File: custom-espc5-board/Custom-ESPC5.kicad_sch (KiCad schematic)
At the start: 43 parts, among them J1 Screw_Terminal_01x02, J10 Barrel_Jack, J12 Conn_01x05, J13 Conn_01x05, J2 Conn_01x03, J3 Conn_01x03, J4 USB_C_Receptacle_USB2.0_14P, J5 Conn_01x03, J6 Screw_Terminal_01x03, SW1 SW_Nidec_CAS-120A1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

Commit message: s3 devboard + imu
austin yun
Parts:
- removed J2, J3: Conn_01x03, Connector_JST:JST_XH_S3B-XH-A-1_1x03_P2.50mm_Horizontal, symbol Connector_Generic:Conn_01x03
- removed U1: ESP32-C5-WROOM-1U, PCM_Espressif:ESP32-C5-WROOM-1U, symbol PCM_Espressif:ESP32-C5-WROOM-1U
- added C8: 10nF, Capacitor_SMD:C_0402_1005Metric, symbol Device:C
- added U1: ICM-42670-P, footprints:LGA14_2.5X3X0.76_IVS, symbol imu:ICM-42670-P
- added U6: ESP32-S3-WROOM-1, RF_Module:ESP32-S3-WROOM-1, symbol RF_Module:ESP32-S3-WROOM-1
- C3: value 0.1µ -> 0.1µF
- C4: value 0.1µ -> 2.2µF
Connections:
- net SIG1 is gone; now on net +3.3V: C3.1
- net SIG2 is gone; now on net +3.3V: C4.1
- net +3.3V: now also C8.1, U1.5 (VDDIO), U1.8 (VDD), U6.2 (3V3)
- net A1: now also U6.20 (IO12)
- net A2: now also U6.19 (IO11)
- net B1: now also U6.8 (IO15)
- net B2: now also U6.7 (IO7)
- net CAN RX: now also U6.39 (IO1)
- net CAN TX: now also U6.38 (IO2)
- net CHIP_PU: now also U6.3 (EN)
- net GND: now also C8.2, U1.6 (GND), U6.1 (GND), U6.40 (GND), U6.41 (GND)
- net IDX1: now also U6.21 (IO13)
- net IDX2: now also U6.9 (IO16)
- net UART RX: now also U6.36 (RXD0)
- net UART TX: now also U6.37 (TXD0)
- net WS2812: now also U6.10 (IO17)
- net GPIO28 renamed GPIO0
- net GPIO0: now also U6.27 (IO0)
- net I2C SCL renamed SCL
- net SCL: now also U1.13 (AP_SCL/AP_SCLK), U6.17 (IO9)
- net I2C SDA renamed SDA
- net SDA: now also U1.14 (AP_SDA/AP_SDIO/AP_SDI), U6.18 (IO10)
- no-connect marks 11 -> 16
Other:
- note added: "IMU"
- note added: "quack"
- note removed: "Analog"
- note removed: "Analog 1"
- note removed: "Analog 2"
- note removed: "Vcc"
- note removed: "wolfwood"
- moved on the sheet: C5, C6, D2, D4, J1, J12, J13, J4, J5, J6, R17, R18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

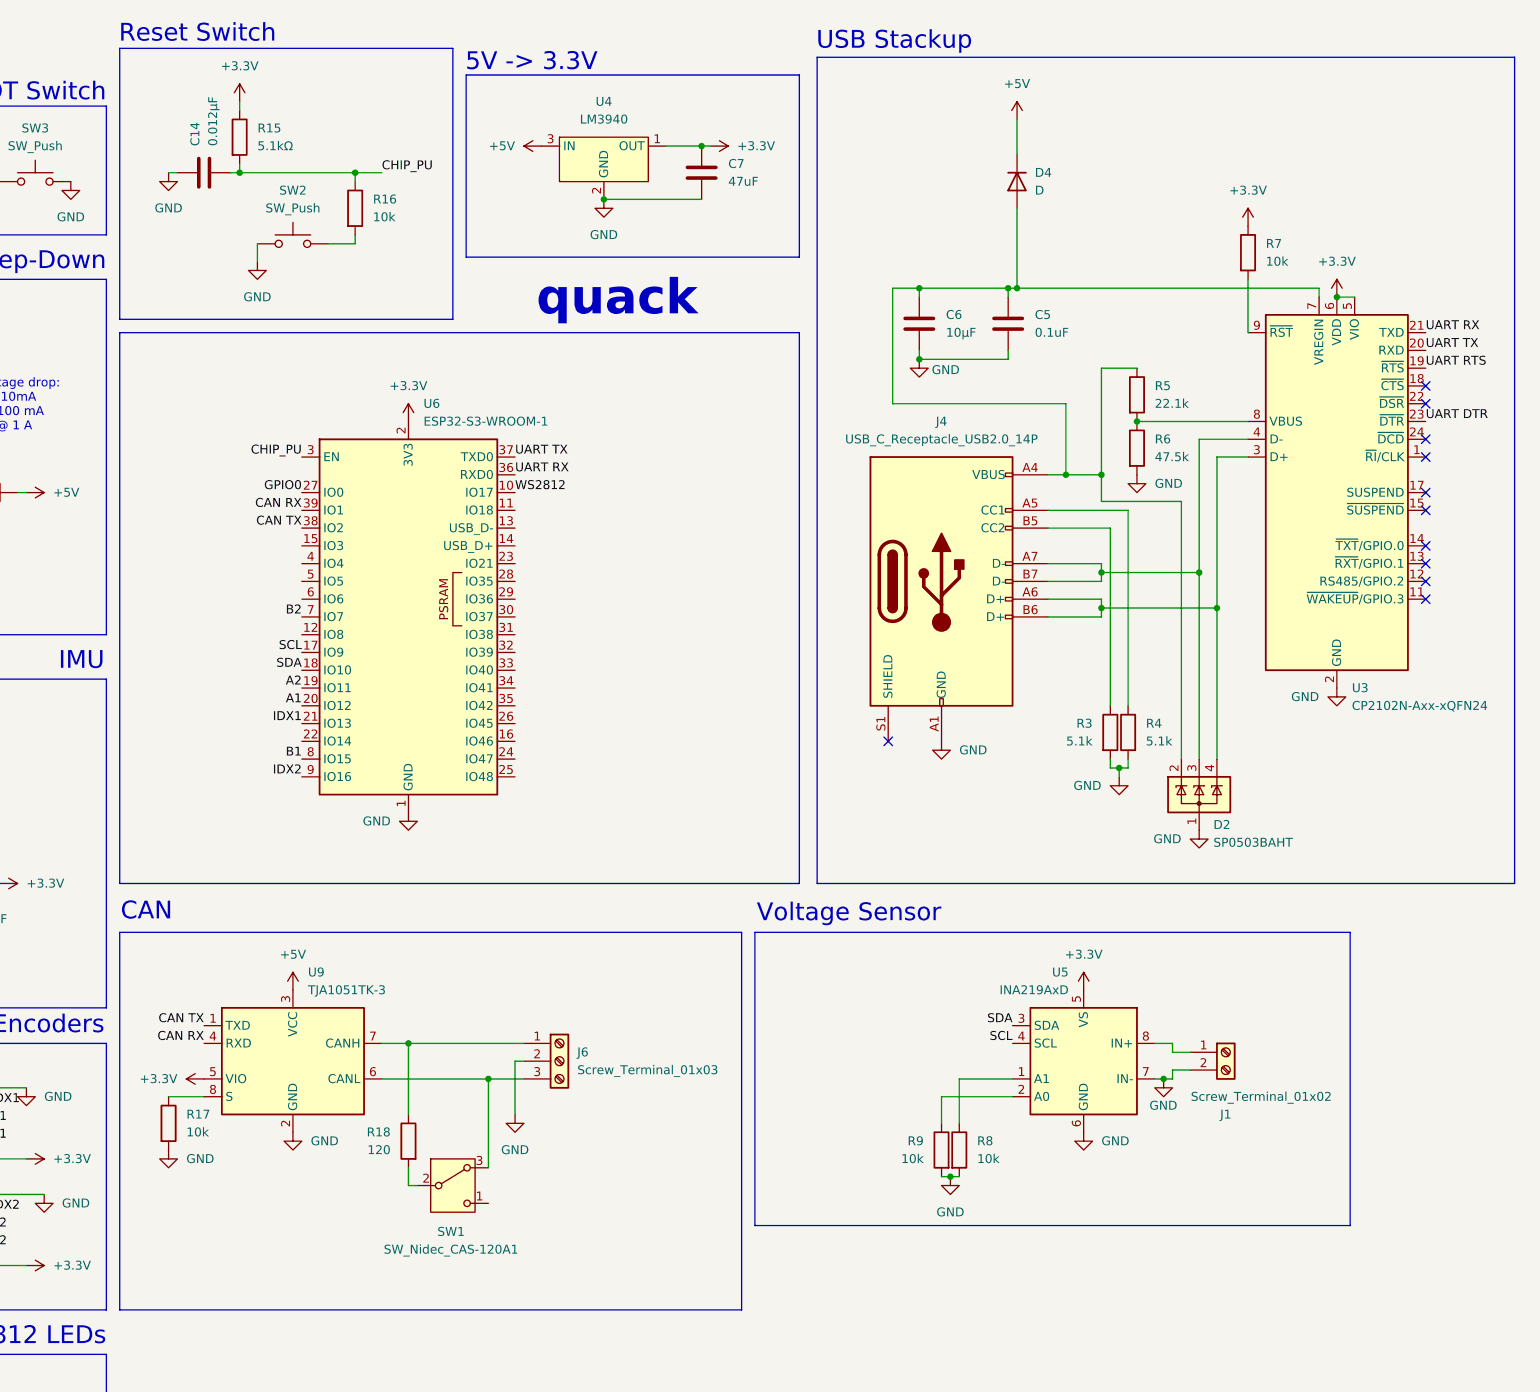
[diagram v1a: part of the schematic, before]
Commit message: Add bypass caps
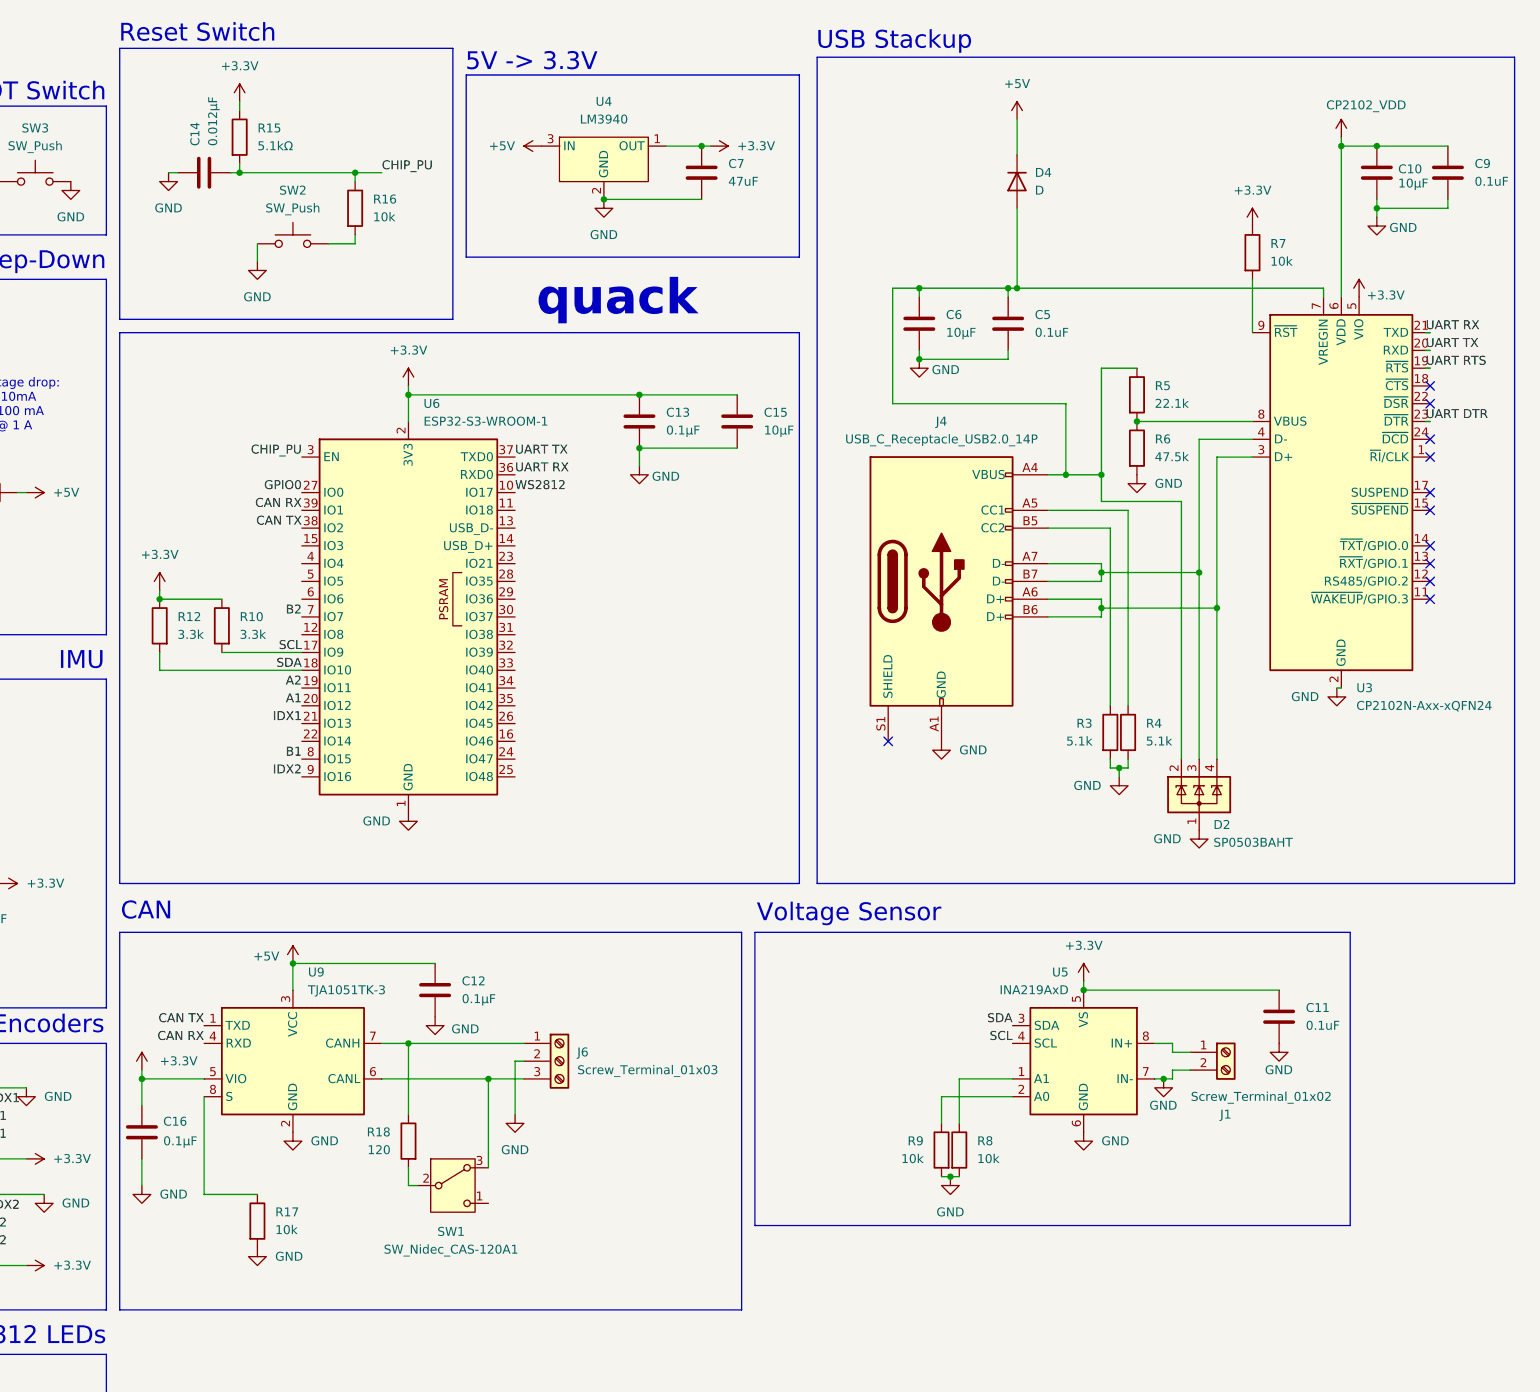
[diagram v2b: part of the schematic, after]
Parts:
- added C10, C15: 10µF, Capacitor_SMD:C_0402_1005Metric, symbol Device:C
- added C11, C9: 0.1uF, Capacitor_SMD:C_0402_1005Metric, symbol Device:C
- added C12, C13, C16: 0.1µF, Capacitor_SMD:C_0402_1005Metric, symbol Device:C
- added R10, R12: 3.3k, Resistor_SMD:R_0402_1005Metric, symbol Device:R
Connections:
- net +3.3V: now also C11.1, C13.1, C15.1, C16.1, R10.1, R12.1; no longer U3.6 (VDD)
- net +5V: now also C12.1
- net GND: now also C10.2, C11.2, C12.2, C13.2, C15.2, C16.2, C9.2
- net SCL: now also R10.2
- net SDA: now also R12.2
- new net CP2102_VDD: C10.1, C9.1, U3.6 (VDD)
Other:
- moved on the sheet: R17, R7, U3

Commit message: Update Custom-ESPC5.kicad_sch
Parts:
- R1: value 910 -> 750
- U2: value LM317DCYR -> LM317KCS; footprint Package_TO_SOT_SMD:SOT-223-3_TabPin2 -> Package_TO_SOT_THT:TO-220-3_Vertical
- U4: value LM3940 -> LM3940IT-3.3; footprint Package_TO_SOT_SMD:SOT-223-3_TabPin2 -> Package_TO_SOT_THT:TO-220-3_Vertical
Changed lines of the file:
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@@
 			)
 		)
-		(property "Value" "910"
+		(property "Value" "750"
 			(at 501.65 332.7399 0)
 			(effects
@@
 			)
 		)
-		(property "Value" "LM3940"
+		(property "Value" "LM3940IT-3.3"
 			(at 609.6 295.91 0)
 			(effects
@@
 			)
 		)
-		(property "Footprint" "Package_TO_SOT_SMD:SOT-223-3_TabPin2"
+		(property "Footprint" "Package_TO_SOT_THT:TO-220-3_Vertical"
 			(at 609.6 297.18 0)
 			(effects
@@
 			)
 		)
-		(property "Value" "LM317DCYR"
+		(property "Value" "LM317KCS"
 			(at 499.11 355.6 0)
 			(effects
@@
 			)
 		)
-		(property "Footprint" "Package_TO_SOT_SMD:SOT-223-3_TabPin2"
+		(property "Footprint" "Package_TO_SOT_THT:TO-220-3_Vertical"
 			(at 499.11 355.6 0)
 			(effects
